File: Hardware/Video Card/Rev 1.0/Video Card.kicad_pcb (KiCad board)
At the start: 2 copper layers, 100 x 57.6 mm, 38 parts, among them J1 INT Select, J2 6502 Card Edge, J3 Conn_02x08_Odd_Even, J4 Video Out, Q1 2N4401, U1 TMS9918A, U2 74HCT574, U3 74HC138, U4 74HC138, U5 74HCT574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

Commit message: Add 3D images for all boards
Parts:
- U1: footprint Package_DIP:DIP-40_W15.24mm_LongPads -> Package_DIP:DIP-40_W15.24mm_Socket_LongPads
- U7: footprint Package_DIP:DIP-28_W15.24mm_LongPads -> Package_DIP:DIP-28_W15.24mm_Socket_LongPads

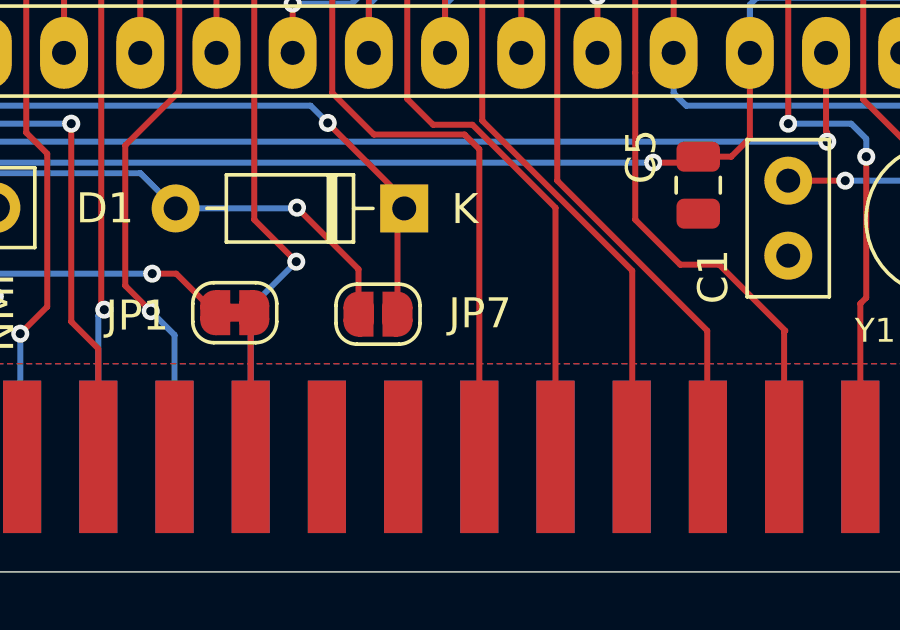
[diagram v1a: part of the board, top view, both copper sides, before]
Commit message: Remove V1.1 of LCD Sound and Video cards
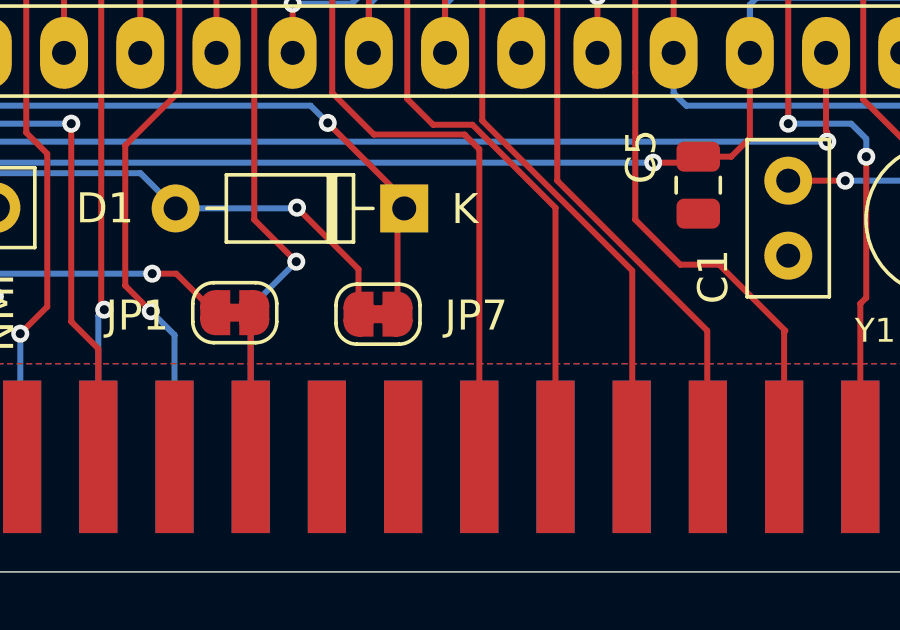
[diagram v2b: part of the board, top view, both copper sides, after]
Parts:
- JP7: footprint Jumper:SolderJumper-2_P1.3mm_Open_RoundedPad1.0x1.5mm -> Jumper:SolderJumper-2_P1.3mm_Bridged_RoundedPad1.0x1.5mm
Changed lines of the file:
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@@
 		(sheetfile "Video Card.kicad_sch")
 		(zone_connect 1)
-		(attr exclude_from_pos_files exclude_from_bom)
+		(attr exclude_from_pos_files exclude_from_bom allow_soldermask_bridges)
+		(fp_rect
+			(start -0.15 -0.75)
+			(end 0.15 0.75)
+			(stroke
+				(width 0)
+				(type default)
+			)
+			(fill yes)
+			(layer "F.Mask")
+		)
 		(fp_line
 			(start -1.4 0.3)
@@
 		(sheetfile "Video Card.kicad_sch")
 		(zone_connect 1)
-		(attr exclude_from_pos_files exclude_from_bom)
+		(attr exclude_from_pos_files exclude_from_bom allow_soldermask_bridges)
+		(fp_rect
+			(start -0.15 -0.75)
+			(end 0.15 0.75)
+			(stroke
+				(width 0)
+				(type default)
+			)
+			(fill yes)
+			(layer "F.Mask")
+		)
 		(fp_line
 			(start 0.7 1)
@@
 		(sheetfile "Video Card.kicad_sch")
 		(zone_connect 1)
-		(attr exclude_from_pos_files exclude_from_bom)
+		(attr exclude_from_pos_files exclude_from_bom allow_soldermask_bridges)
 		(net_tie_pad_groups "1, 2")
 		(fp_poly
@@
 			(layer "F.Cu")
 		)
+		(fp_rect
+			(start -0.15 -0.75)
+			(end 0.15 0.75)
+			(stroke
+				(width 0)
+				(type default)
+			)
+			(fill yes)
+			(layer "F.Mask")
+		)
 		(fp_line
 			(start -1.4 0.3)
@@
 		(sheetfile "Video Card.kicad_sch")
 		(zone_connect 1)
-		(attr exclude_from_pos_files exclude_from_bom)
+		(attr exclude_from_pos_files exclude_from_bom allow_soldermask_bridges)
 		(net_tie_pad_groups "1, 2")
 		(fp_poly
@@
 			(layer "F.Cu")
 		)
+		(fp_rect
+			(start -0.15 -0.75)
+			(end 0.15 0.75)
+			(stroke
+				(width 0)
+				(type default)
+			)
+			(fill yes)
+			(layer "F.Mask")
+		)
 		(fp_line
 			(start 1.4 -0.3)
@@
 		(sheetfile "Video Card.kicad_sch")
 		(zone_connect 1)
-		(attr exclude_from_pos_files exclude_from_bom)
+		(attr exclude_from_pos_files exclude_from_bom allow_soldermask_bridges)
+		(fp_rect
+			(start -0.15 -0.75)
+			(end 0.15 0.75)
+			(stroke
+				(width 0)
+				(type default)
+			)
+			(fill yes)
+			(layer "F.Mask")
+		)
 		(fp_line
 			(start -1.4 0.3)
@@
 		(sheetfile "Video Card.kicad_sch")
 		(zone_connect 1)
-		(attr exclude_from_pos_files exclude_from_bom)
+		(attr exclude_from_pos_files exclude_from_bom allow_soldermask_bridges)
 		(net_tie_pad_groups "1, 2")
 		(fp_poly
@@
 			(layer "F.Cu")
 		)
+		(fp_rect
+			(start -0.15 -0.75)
+			(end 0.15 0.75)
+			(stroke
+				(width 0)
+				(type default)
+			)
+			(fill yes)
+			(layer "F.Mask")
+		)
 		(fp_line
 			(start -1.4 0.3)
@@
 		)
 	)
-	(footprint "Jumper:SolderJumper-2_P1.3mm_Open_RoundedPad1.0x1.5mm"
+	(footprint "Jumper:SolderJumper-2_P1.3mm_Bridged_RoundedPad1.0x1.5mm"
 		(layer "F.Cu")
 		(at 131.125 119.35 180)
-		(descr "SMD Solder Jumper, 1x1.5mm, rounded Pads, 0.3mm gap, open")
-		(tags "solder jumper open")
+		(descr "SMD Solder Jumper, 1x1.5mm, rounded Pads, 0.3mm gap, bridged with 1 copper strip")
+		(tags "net tie solder jumper bridged")
 		(property "Reference" "JP7"
-			(at -3.4 0.025 180)
+			(at -3.275 -0.05 180)
 			(layer "F.SilkS")
 			(effects
@@
 			)
 		)
-		(property "Description" "Solder Jumper, 2-pole, open"
+		(property "Description" "Solder Jumper, 2-pole, closed/bridged"
 			(at 0 0 180)
 			(unlocked yes)
@@
 			)
 		)
-		(property ki_fp_filters "SolderJumper*Open*")
+		(property ki_fp_filters "SolderJumper*Bridged*")
 		(sheetname "/")
 		(sheetfile "Video Card.kicad_sch")
 		(zone_connect 1)
-		(attr exclude_from_pos_files exclude_from_bom)
+		(attr exclude_from_pos_files exclude_from_bom allow_soldermask_bridges)
+		(net_tie_pad_groups "1, 2")
+		(fp_poly
+			(pts
+				(xy 0.25 -0.3) (xy -0.25 -0.3) (xy -0.25 0.3) (xy 0.25 0.3)
+			)
+			(stroke
+				(width 0)
+				(type solid)
+			)
+			(fill yes)
+			(layer "F.Cu")
+		)
+		(fp_rect
+			(start -0.15 -0.75)
+			(end 0.15 0.75)
+			(stroke
+				(width 0)
+				(type default)
+			)
+			(fill yes)
+			(layer "F.Mask")
+		)
 		(fp_line
 			(start 1.4 -0.3)

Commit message: Cleanup for production
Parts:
- J4: value Video Out -> VIDEO
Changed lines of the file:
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@@
 			)
 		)
-		(property "Value" "Video Out"
-			(at 6.375 -2.75 180)
+		(property "Value" "VIDEO"
+			(at 6.33 -4 180)
 			(layer "F.SilkS")
 			(effects
